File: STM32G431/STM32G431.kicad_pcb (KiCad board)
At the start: 4 copper layers, 60 x 44 mm, 154 parts, among them J1 W, J10 NTC, J11 LED, J2 U, J3 V, J4 GND, J5 VIN, J6 UART, J8 HALL, J9 AIN/PWM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

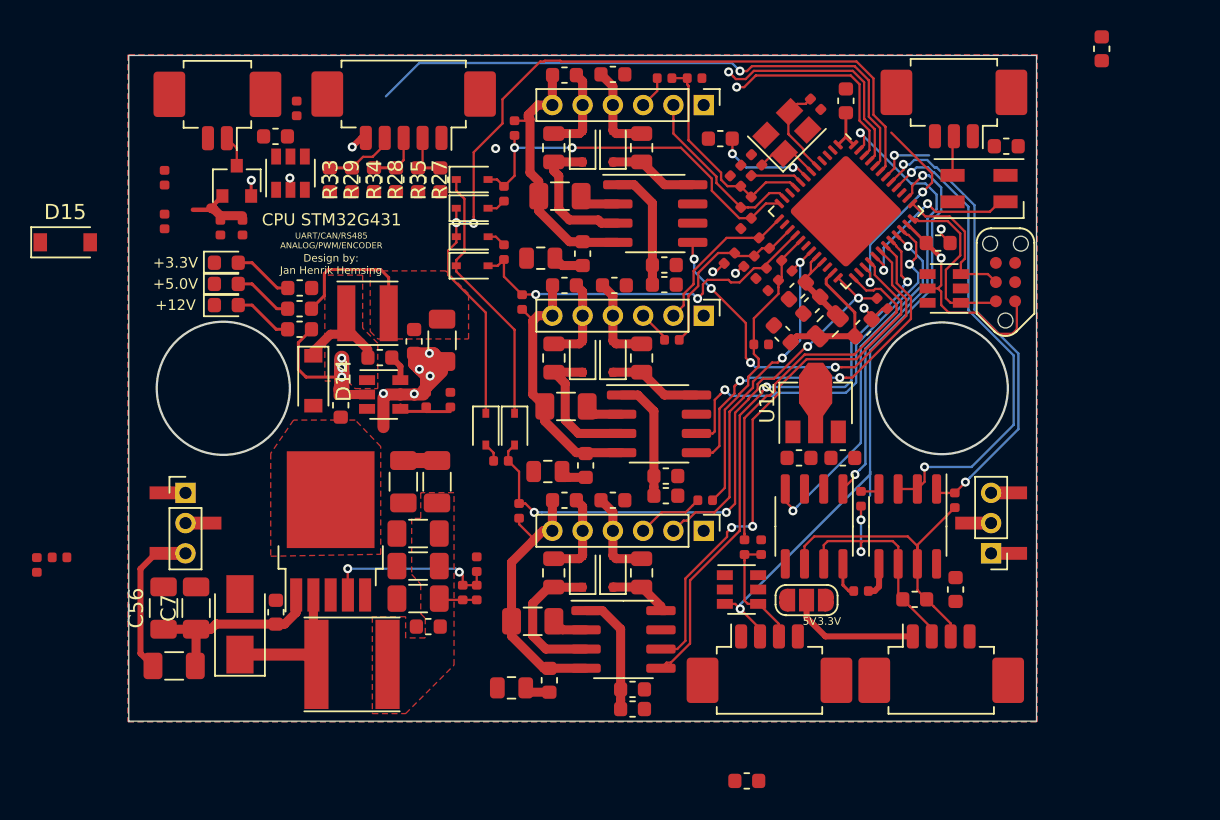
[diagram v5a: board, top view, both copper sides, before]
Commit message: updated layout
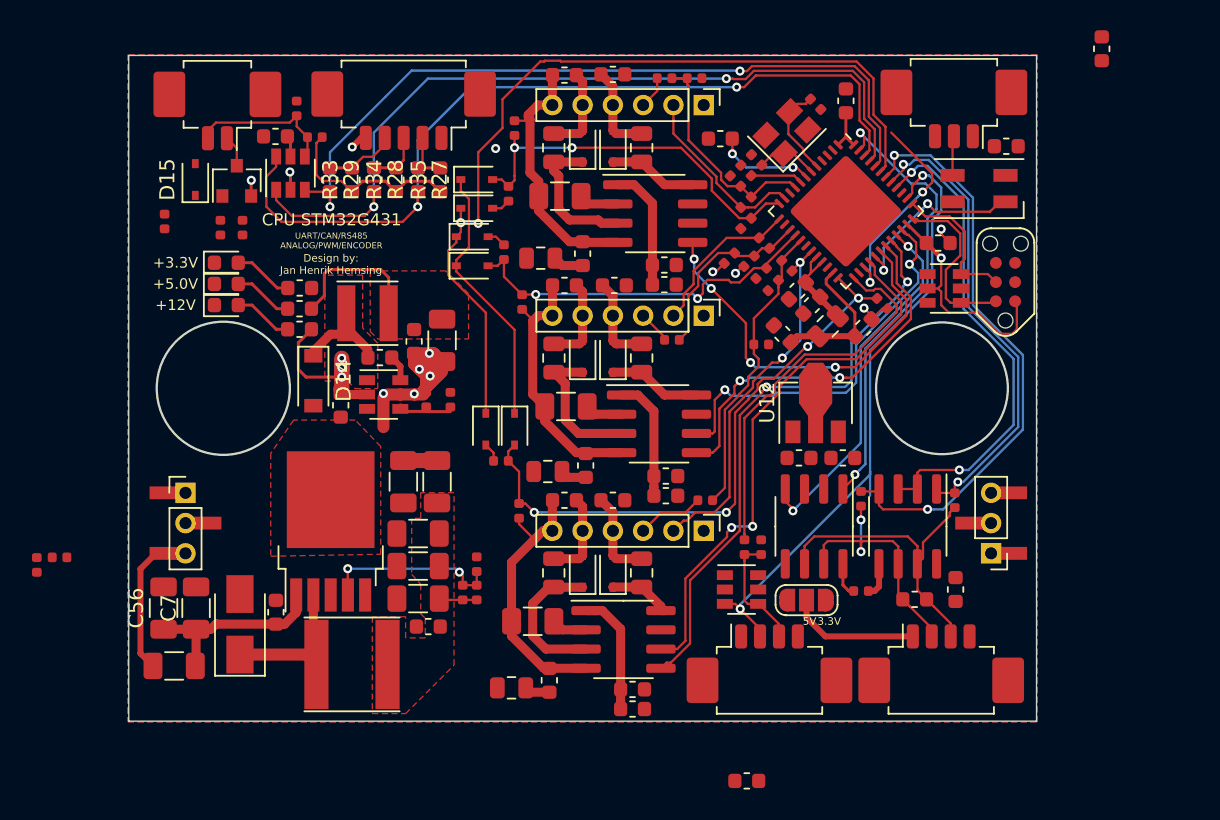
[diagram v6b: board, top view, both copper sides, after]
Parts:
- D15: value B5819W -> 1N5819WS; footprint Diode_SMD:D_SOD-123 -> Diode_SMD:D_SOD-323
- moved R20 10.3 mm to (32.3, 28.4), turned to 180 degrees
- moved D15 9.55 mm to (24.4, 31.2), turned to 90 degrees
- moved R31 0.30 mm to (45.1, 32.1)
- moved D10 0.30 mm to (43.0, 31.2)
- moved D13 0.30 mm to (43.0, 33.1)
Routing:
- net HALL1: track 13.8 -> 56.1 mm, vias 1 -> 2
- net HALL2: track 15.3 -> 53.8 mm, vias 1 -> 2
- net UART_RX: track 5.21 -> 38.8 mm, vias 1 -> 2
- net +3V3: track 46.1 -> 58.6 mm
- net HALL3: track 39.7 -> 50.8 mm, vias 1 -> 2
- net NTC_EXT: track 0.00 -> 9.84 mm
- net Net-(C40-Pad1): track 5.08 -> 0.00 mm
- net +5V: track 9.62 -> 11.0 mm

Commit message: updated layout
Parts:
- moved R21 5.45 mm to (22.5, 32.2), turned to 180 degrees
- moved C40 4.71 mm to (22.5, 31.3), turned to 180 degrees
- moved C39 3.62 mm to (22.5, 30.4), turned to 180 degrees
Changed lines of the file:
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@@
   )
   (setup
-    (last_trace_width 0.154)
+    (last_trace_width 0.2)
     (user_trace_width 0.154)
     (user_trace_width 0.2)
@@
   )
   (module Resistor_SMD:R_0402_1005Metric (layer F.Cu)
-    (at 27.52 34.38 270)
+    (at 22.5 32.25 180)
     (descr "Resistor SMD 0402 (1005 Metric), square (rectangular) end terminal, IPC_7351 nominal, (Body size source: http://www.tortai-tech.com/upload/download/2011102023233369053.pdf), generated with kicad-footprint-generator")
     (tags resistor)
     (attr smd)
-    (fp_text reference R21 (at 0 -1.17 90) (layer F.SilkS) hide
-      (effects (font (size 0.5 0.5) (thickness 0.14)))
-    )
-    (fp_text value 1M (at 0 1.17 90) (layer F.Fab)
-      (effects (font (size 1 1) (thickness 0.15)))
-    )
-    (fp_text user %R (at 0 0 90) (layer F.Fab) hide
-      (effects (font (size 0.5 0.5) (thickness 0.14)))
-    )
-    (fp_line (start 0.93 0.47) (end -0.93 0.47) (layer F.CrtYd) (width 0.05))
-    (fp_line (start 0.93 -0.47) (end 0.93 0.47) (layer F.CrtYd) (width 0.05))
-    (fp_line (start -0.93 -0.47) (end 0.93 -0.47) (layer F.CrtYd) (width 0.05))
-    (fp_line (start -0.93 0.47) (end -0.93 -0.47) (layer F.CrtYd) (width 0.05))
-    (fp_line (start 0.5 0.25) (end -0.5 0.25) (layer F.Fab) (width 0.1))
-    (fp_line (start 0.5 -0.25) (end 0.5 0.25) (layer F.Fab) (width 0.1))
-    (fp_line (start -0.5 -0.25) (end 0.5 -0.25) (layer F.Fab) (width 0.1))
-    (fp_line (start -0.5 0.25) (end -0.5 -0.25) (layer F.Fab) (width 0.1))
-    (pad 2 smd roundrect (at 0.485 0 270) (size 0.59 0.64) (layers F.Cu F.Paste F.Mask) (roundrect_rratio 0.25)
+    (fp_text reference R21 (at 0 -1.17) (layer F.SilkS) hide
+      (effects (font (size 0.5 0.5) (thickness 0.14)))
+    )
+    (fp_text value 1M (at 0 1.17) (layer F.Fab)
+      (effects (font (size 1 1) (thickness 0.15)))
+    )
+    (fp_text user %R (at 0 0) (layer F.Fab) hide
+      (effects (font (size 0.5 0.5) (thickness 0.14)))
+    )
+    (fp_line (start 0.93 0.47) (end -0.93 0.47) (layer F.CrtYd) (width 0.05))
+    (fp_line (start 0.93 -0.47) (end 0.93 0.47) (layer F.CrtYd) (width 0.05))
+    (fp_line (start -0.93 -0.47) (end 0.93 -0.47) (layer F.CrtYd) (width 0.05))
+    (fp_line (start -0.93 0.47) (end -0.93 -0.47) (layer F.CrtYd) (width 0.05))
+    (fp_line (start 0.5 0.25) (end -0.5 0.25) (layer F.Fab) (width 0.1))
+    (fp_line (start 0.5 -0.25) (end 0.5 0.25) (layer F.Fab) (width 0.1))
+    (fp_line (start -0.5 -0.25) (end 0.5 -0.25) (layer F.Fab) (width 0.1))
+    (fp_line (start -0.5 0.25) (end -0.5 -0.25) (layer F.Fab) (width 0.1))
+    (pad 2 smd roundrect (at 0.485 0 180) (size 0.59 0.64) (layers F.Cu F.Paste F.Mask) (roundrect_rratio 0.25)
       (net 10 GND))
-    (pad 1 smd roundrect (at -0.485 0 270) (size 0.59 0.64) (layers F.Cu F.Paste F.Mask) (roundrect_rratio 0.25)
+    (pad 1 smd roundrect (at -0.485 0 180) (size 0.59 0.64) (layers F.Cu F.Paste F.Mask) (roundrect_rratio 0.25)
       (net 45 "Net-(C40-Pad1)"))
     (model ${KISYS3DMOD}/Resistor_SMD.3dshapes/R_0402_1005Metric.wrl
@@
   )
   (module Resistor_SMD:R_0402_1005Metric (layer F.Cu)
-    (at 26.06 34.38 270)
+    (at 22.5 31.3 180)
     (descr "Resistor SMD 0402 (1005 Metric), square (rectangular) end terminal, IPC_7351 nominal, (Body size source: http://www.tortai-tech.com/upload/download/2011102023233369053.pdf), generated with kicad-footprint-generator")
     (tags resistor)
     (attr smd)
-    (fp_text reference C40 (at 0 -1.17 90) (layer F.SilkS) hide
-      (effects (font (size 0.5 0.5) (thickness 0.14)))
-    )
-    (fp_text value 100p (at 0 1.17 90) (layer F.Fab)
-      (effects (font (size 1 1) (thickness 0.15)))
-    )
-    (fp_text user %R (at 0 0 90) (layer F.Fab) hide
-      (effects (font (size 0.5 0.5) (thickness 0.14)))
-    )
-    (fp_line (start 0.93 0.47) (end -0.93 0.47) (layer F.CrtYd) (width 0.05))
-    (fp_line (start 0.93 -0.47) (end 0.93 0.47) (layer F.CrtYd) (width 0.05))
-    (fp_line (start -0.93 -0.47) (end 0.93 -0.47) (layer F.CrtYd) (width 0.05))
-    (fp_line (start -0.93 0.47) (end -0.93 -0.47) (layer F.CrtYd) (width 0.05))
-    (fp_line (start 0.5 0.25) (end -0.5 0.25) (layer F.Fab) (width 0.1))
-    (fp_line (start 0.5 -0.25) (end 0.5 0.25) (layer F.Fab) (width 0.1))
-    (fp_line (start -0.5 -0.25) (end 0.5 -0.25) (layer F.Fab) (width 0.1))
-    (fp_line (start -0.5 0.25) (end -0.5 -0.25) (layer F.Fab) (width 0.1))
-    (pad 2 smd roundrect (at 0.485 0 270) (size 0.59 0.64) (layers F.Cu F.Paste F.Mask) (roundrect_rratio 0.25)
+    (fp_text reference C40 (at 0 -1.17) (layer F.SilkS) hide
+      (effects (font (size 0.5 0.5) (thickness 0.14)))
+    )
+    (fp_text value 100p (at 0 1.17) (layer F.Fab)
+      (effects (font (size 1 1) (thickness 0.15)))
+    )
+    (fp_text user %R (at 0 0) (layer F.Fab) hide
+      (effects (font (size 0.5 0.5) (thickness 0.14)))
+    )
+    (fp_line (start 0.93 0.47) (end -0.93 0.47) (layer F.CrtYd) (width 0.05))
+    (fp_line (start 0.93 -0.47) (end 0.93 0.47) (layer F.CrtYd) (width 0.05))
+    (fp_line (start -0.93 -0.47) (end 0.93 -0.47) (layer F.CrtYd) (width 0.05))
+    (fp_line (start -0.93 0.47) (end -0.93 -0.47) (layer F.CrtYd) (width 0.05))
+    (fp_line (start 0.5 0.25) (end -0.5 0.25) (layer F.Fab) (width 0.1))
+    (fp_line (start 0.5 -0.25) (end 0.5 0.25) (layer F.Fab) (width 0.1))
+    (fp_line (start -0.5 -0.25) (end 0.5 -0.25) (layer F.Fab) (width 0.1))
+    (fp_line (start -0.5 0.25) (end -0.5 -0.25) (layer F.Fab) (width 0.1))
+    (pad 2 smd roundrect (at 0.485 0 180) (size 0.59 0.64) (layers F.Cu F.Paste F.Mask) (roundrect_rratio 0.25)
       (net 10 GND))
-    (pad 1 smd roundrect (at -0.485 0 270) (size 0.59 0.64) (layers F.Cu F.Paste F.Mask) (roundrect_rratio 0.25)
+    (pad 1 smd roundrect (at -0.485 0 180) (size 0.59 0.64) (layers F.Cu F.Paste F.Mask) (roundrect_rratio 0.25)
       (net 45 "Net-(C40-Pad1)"))
     (model ${KISYS3DMOD}/Resistor_SMD.3dshapes/R_0402_1005Metric.wrl
@@
   )
   (module Resistor_SMD:R_0402_1005Metric (layer F.Cu)
-    (at 22.37 33.972499 270)
+    (at 22.5 30.35 180)
     (descr "Resistor SMD 0402 (1005 Metric), square (rectangular) end terminal, IPC_7351 nominal, (Body size source: http://www.tortai-tech.com/upload/download/2011102023233369053.pdf), generated with kicad-footprint-generator")
     (tags resistor)
     (attr smd)
-    (fp_text reference C39 (at 0 -1.17 90) (layer F.SilkS) hide
-      (effects (font (size 0.5 0.5) (thickness 0.14)))
-    )
-    (fp_text value 100p (at 0 1.17 90) (layer F.Fab)
-      (effects (font (size 1 1) (thickness 0.15)))
-    )
-    (fp_text user %R (at 0 0 90) (layer F.Fab) hide
-      (effects (font (size 0.5 0.5) (thickness 0.14)))
-    )
-    (fp_line (start 0.93 0.47) (end -0.93 0.47) (layer F.CrtYd) (width 0.05))
-    (fp_line (start 0.93 -0.47) (end 0.93 0.47) (layer F.CrtYd) (width 0.05))
-    (fp_line (start -0.93 -0.47) (end 0.93 -0.47) (layer F.CrtYd) (width 0.05))
-    (fp_line (start -0.93 0.47) (end -0.93 -0.47) (layer F.CrtYd) (width 0.05))
-    (fp_line (start 0.5 0.25) (end -0.5 0.25) (layer F.Fab) (width 0.1))
-    (fp_line (start 0.5 -0.25) (end 0.5 0.25) (layer F.Fab) (width 0.1))
-    (fp_line (start -0.5 -0.25) (end 0.5 -0.25) (layer F.Fab) (width 0.1))
-    (fp_line (start -0.5 0.25) (end -0.5 -0.25) (layer F.Fab) (width 0.1))
-    (pad 2 smd roundrect (at 0.485 0 270) (size 0.59 0.64) (layers F.Cu F.Paste F.Mask) (roundrect_rratio 0.25)
+    (fp_text reference C39 (at 0 -1.17) (layer F.SilkS) hide
+      (effects (font (size 0.5 0.5) (thickness 0.14)))
+    )
+    (fp_text value 100p (at 0 1.17) (layer F.Fab)
+      (effects (font (size 1 1) (thickness 0.15)))
+    )
+    (fp_text user %R (at 0 0) (layer F.Fab) hide
+      (effects (font (size 0.5 0.5) (thickness 0.14)))
+    )
+    (fp_line (start 0.93 0.47) (end -0.93 0.47) (layer F.CrtYd) (width 0.05))
+    (fp_line (start 0.93 -0.47) (end 0.93 0.47) (layer F.CrtYd) (width 0.05))
+    (fp_line (start -0.93 -0.47) (end 0.93 -0.47) (layer F.CrtYd) (width 0.05))
+    (fp_line (start -0.93 0.47) (end -0.93 -0.47) (layer F.CrtYd) (width 0.05))
+    (fp_line (start 0.5 0.25) (end -0.5 0.25) (layer F.Fab) (width 0.1))
+    (fp_line (start 0.5 -0.25) (end 0.5 0.25) (layer F.Fab) (width 0.1))
+    (fp_line (start -0.5 -0.25) (end 0.5 -0.25) (layer F.Fab) (width 0.1))
+    (fp_line (start -0.5 0.25) (end -0.5 -0.25) (layer F.Fab) (width 0.1))
+    (pad 2 smd roundrect (at 0.485 0 180) (size 0.59 0.64) (layers F.Cu F.Paste F.Mask) (roundrect_rratio 0.25)
       (net 10 GND))
-    (pad 1 smd roundrect (at -0.485 0 270) (size 0.59 0.64) (layers F.Cu F.Paste F.Mask) (roundrect_rratio 0.25)
+    (pad 1 smd roundrect (at -0.485 0 180) (size 0.59 0.64) (layers F.Cu F.Paste F.Mask) (roundrect_rratio 0.25)
       (net 40 NTC_EXT))
     (model ${KISYS3DMOD}/Resistor_SMD.3dshapes/R_0402_1005Metric.wrl

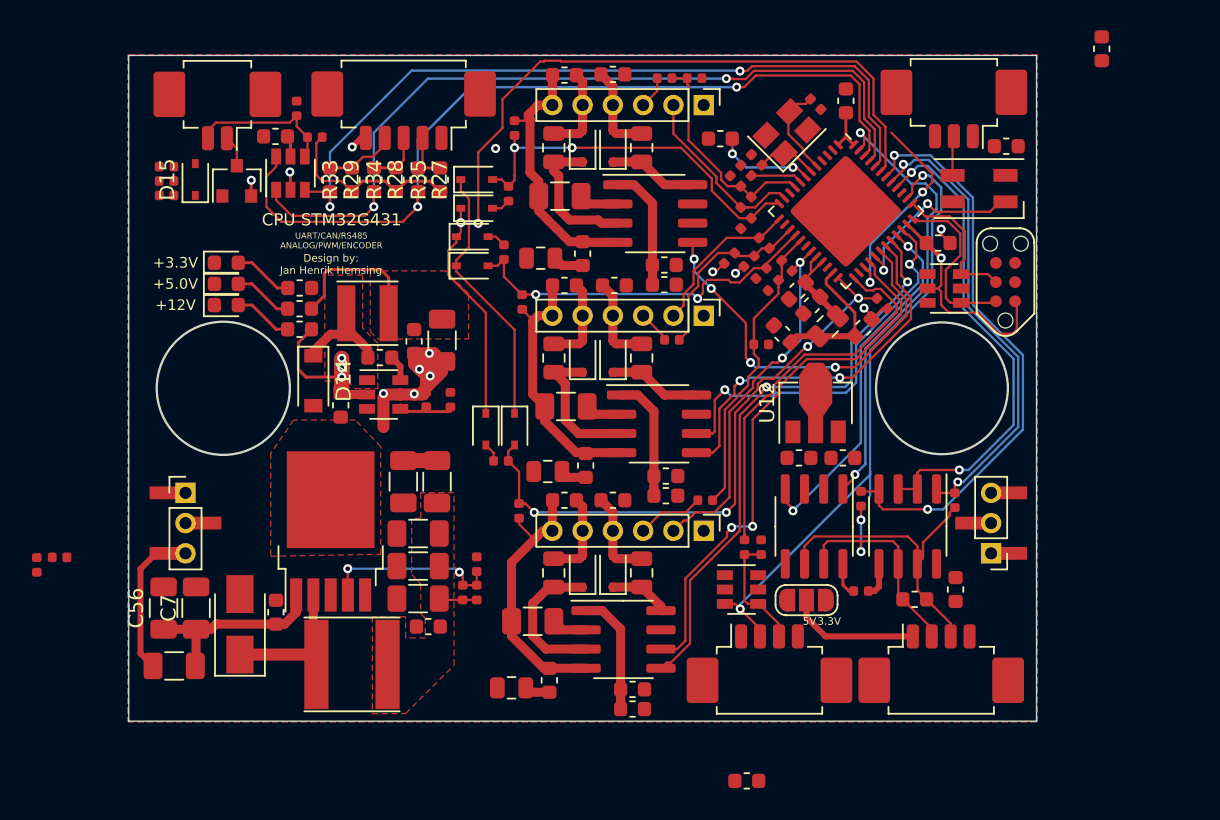
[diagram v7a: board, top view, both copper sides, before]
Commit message: updated layout
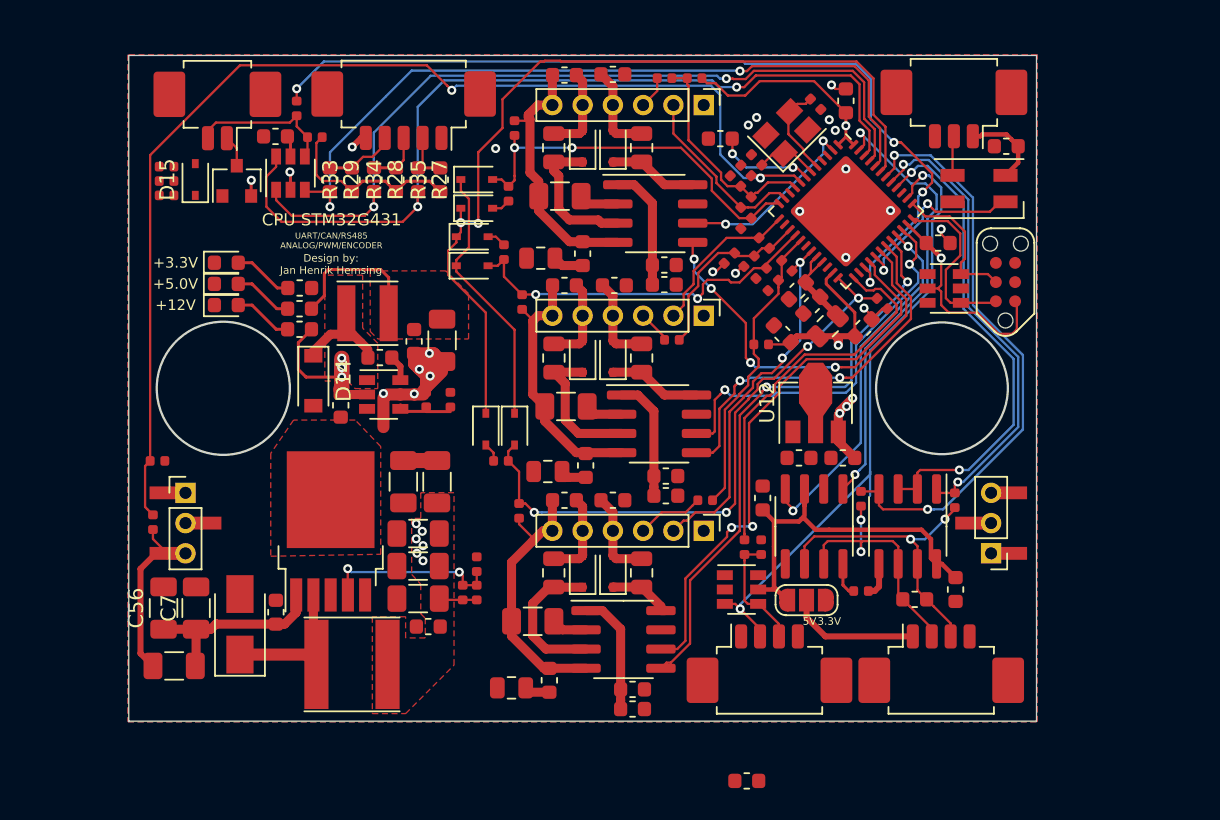
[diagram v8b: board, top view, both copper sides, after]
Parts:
- moved C10 37.2 mm to (61.9, 52.2)
- moved R17 10.5 mm to (21.9, 49.8), turned to 0 degrees
- moved R6 6.60 mm to (21.6, 53.9), turned to 90 degrees
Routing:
- net Vin_mon: track 3.45 -> 76.2 mm, vias 0 -> 2
- net +3V3: track 58.6 -> 115.8 mm, vias 2 -> 7
- net NTC_IO: track 13.8 -> 58.2 mm, vias 2 -> 4
- net +5V: track 11.0 -> 41.9 mm
- net WL: track 0.00 -> 12.3 mm, vias 0 -> 2
- net VIN: track 10.2 -> 12.1 mm
- net HALL1: track 56.1 -> 57.8 mm
- net GND: track 31.3 -> 32.4 mm, vias 12 -> 21
- net CANL: track 20.2 -> 19.3 mm, vias 0 -> 2
- net +12V: vias 3 -> 9
